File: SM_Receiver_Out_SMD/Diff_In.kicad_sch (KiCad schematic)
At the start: 9 parts, among them J7 RJ45, J8 RJ45, SW2 Terminators, U3 AM26C32IN

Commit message: working on BOM
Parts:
- added R2: 100K, Resistor_SMD:R_0603_1608Metric_Pad0.98x0.95mm_HandSolder, symbol Device:R
- J7, J8: LCSC_PN (none) -> C305972
- SW2: Digi-Key_PN (none) -> 2223-DS04-254-1L-04BK-ND; LCSC_PN (none) -> C509571; MPN (none) -> DS04-254-1L-04BK
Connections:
- net GND: now also R2.2; no longer U3.12 (EN_2)
- new net DIFF_EN: R2.1, U3.12 (EN_2)
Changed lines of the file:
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@@
     (stroke (width 0) (type default) (color 0 0 0 0))
   )
-  (wire (pts (xy 109.855 116.84) (xy 109.855 128.905))
+  (wire (pts (xy 108.204 116.84) (xy 121.92 116.84))
     (stroke (width 0) (type default) (color 0 0 0 0))
   )
-  (wire (pts (xy 121.92 116.84) (xy 109.855 116.84))
-    (stroke (width 0) (type default) (color 0 0 0 0))
-  )
   (global_label "Serial1_P" (shape input) (at 121.92 121.92 180) (fields_autoplaced)
     (effects (font (size 1.27 1.27)) (justify right))
@@
     (property "Intersheet References" "${INTERSHEET_REFS}" (id 0) (at 229.7147 62.3094 0)
       (effects (font (size 1.27 1.27)) (justify left) hide)
+    )
+  )
+  (global_label "DIFF_EN" (shape input) (at 108.204 116.84 180) (fields_autoplaced)
+    (effects (font (size 1.27 1.27)) (justify right))
+    (property "Intersheet References" "${INTERSHEET_REFS}" (id 0) (at 98.3808 116.7606 0)
+      (effects (font (size 1.27 1.27)) (justify right) hide)
     )
   )
@@
       (effects (font (size 1.27 1.27)) hide)
     )
+    (property "LCSC_PN" "C305972" (id 6) (at 147.32 53.34 0)
+      (effects (font (size 1.27 1.27)) hide)
+    )
     (pin "1")
     (pin "2")
@@
     (pin "8")
   )
-  (symbol (lib_id "power:GND") (at 109.855 128.905 0) (mirror y) (unit 1)
-    (in_bom yes) (on_board yes) (fields_autoplaced)
-    (property "Reference" "#PWR018" (id 0) (at 109.855 135.255 0)
-      (effects (font (size 1.27 1.27)) hide)
-    )
-    (property "Value" "GND" (id 1) (at 109.855 134.493 0))
-    (property "Footprint" "" (id 2) (at 109.855 128.905 0)
-      (effects (font (size 1.27 1.27)) hide)
-    )
-    (property "Datasheet" "" (id 3) (at 109.855 128.905 0)
+  (symbol (lib_id "power:GND") (at 108.204 124.46 0) (mirror y) (unit 1)
+    (in_bom yes) (on_board yes)
+    (property "Reference" "#PWR018" (id 0) (at 108.204 130.81 0)
+      (effects (font (size 1.27 1.27)) hide)
+    )
+    (property "Value" "GND" (id 1) (at 108.204 128.27 0))
+    (property "Footprint" "" (id 2) (at 108.204 124.46 0)
+      (effects (font (size 1.27 1.27)) hide)
+    )
+    (property "Datasheet" "" (id 3) (at 108.204 124.46 0)
       (effects (font (size 1.27 1.27)) hide)
     )
@@
     (pin "2")
   )
+  (symbol (lib_id "Device:R") (at 108.204 120.65 0) (unit 1)
+    (in_bom yes) (on_board yes)
+    (property "Reference" "R2" (id 0) (at 102.108 120.142 0)
+      (effects (font (size 1.27 1.27)) (justify left))
+    )
+    (property "Value" "100K" (id 1) (at 101.346 122.174 0)
+      (effects (font (size 1.27 1.27)) (justify left))
+    )
+    (property "Footprint" "Resistor_SMD:R_0603_1608Metric_Pad0.98x0.95mm_HandSolder" (id 2) (at 106.426 120.65 90)
+      (effects (font (size 1.27 1.27)) hide)
+    )
+    (property "Datasheet" "~" (id 3) (at 108.204 120.65 0)
+      (effects (font (size 1.27 1.27)) hide)
+    )
+    (property "Digi-Key_PN" "YAG1235CT-ND" (id 4) (at 108.204 120.65 0)
+      (effects (font (size 1.27 1.27)) hide)
+    )
+    (property "LCSC_PN" "C25803" (id 5) (at 108.204 120.65 0)
+      (effects (font (size 1.27 1.27)) hide)
+    )
+    (property "MPN" "RT0603BRD07100KL" (id 6) (at 108.204 120.65 0)
+      (effects (font (size 1.27 1.27)) hide)
+    )
+    (pin "1")
+    (pin "2")
+  )
   (symbol (lib_id "power:+3.3V") (at 186.055 104.775 0) (mirror y) (unit 1)
     (in_bom yes) (on_board yes) (fields_autoplaced)
@@
     )
     (property "Datasheet" "~" (id 3) (at 203.2 67.31 0)
+      (effects (font (size 1.27 1.27)) hide)
+    )
+    (property "Digi-Key_PN" "2223-DS04-254-1L-04BK-ND" (id 4) (at 203.2 67.31 0)
+      (effects (font (size 1.27 1.27)) hide)
+    )
+    (property "LCSC_PN" "C509571" (id 5) (at 203.2 67.31 0)
+      (effects (font (size 1.27 1.27)) hide)
+    )
+    (property "MPN" "DS04-254-1L-04BK" (id 6) (at 203.2 67.31 0)
       (effects (font (size 1.27 1.27)) hide)
     )
@@
       (effects (font (size 1.27 1.27)) hide)
     )
+    (property "LCSC_PN" "C305972" (id 6) (at 111.76 53.34 0)
+      (effects (font (size 1.27 1.27)) hide)
+    )

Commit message: fixing I2C lines were backwards
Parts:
- C4: Digi-Key_PN 1292-1630-1-ND -> 1276-1935-2-ND; LCSC_PN C1525 -> C14663; MPN 0402B104K160CT -> CL10B104KB8NNWC
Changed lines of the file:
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@@
       (effects (font (size 1.27 1.27)) hide)
     )
-    (property "Digi-Key_PN" "1292-1630-1-ND" (id 4) (at 186.055 108.585 0)
+    (property "Digi-Key_PN" "1276-1935-2-ND" (id 4) (at 186.055 108.585 0)
       (effects (font (size 1.27 1.27)) hide)
     )
-    (property "MPN" "0402B104K160CT" (id 5) (at 186.055 108.585 0)
+    (property "MPN" "CL10B104KB8NNWC" (id 5) (at 186.055 108.585 0)
       (effects (font (size 1.27 1.27)) hide)
     )
-    (property "LCSC_PN" "C1525" (id 6) (at 186.055 108.585 0)
+    (property "LCSC_PN" "C14663" (id 6) (at 186.055 108.585 0)
       (effects (font (size 1.27 1.27)) hide)
     )

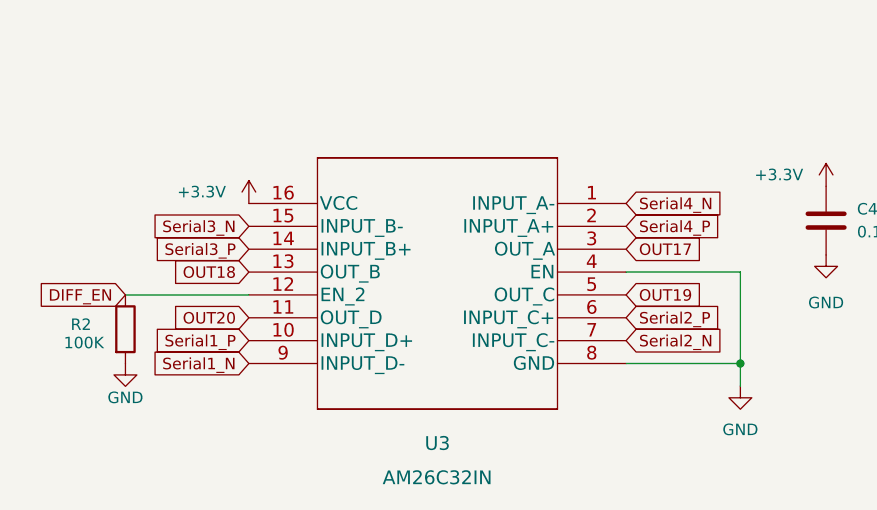
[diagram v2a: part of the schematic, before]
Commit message: fix miswired serial receiver
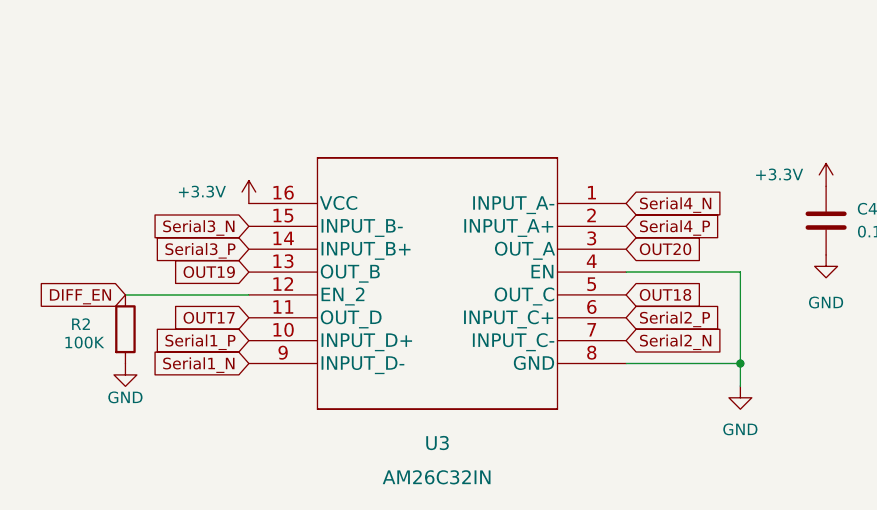
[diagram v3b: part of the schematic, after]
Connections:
- net OUT17: now also U3.11 (OUT_D); no longer U3.3 (OUT_A)
- net OUT18: now also U3.5 (OUT_C); no longer U3.13 (OUT_B)
- net OUT19: now also U3.13 (OUT_B); no longer U3.5 (OUT_C)
- net OUT20: now also U3.3 (OUT_A); no longer U3.11 (OUT_D)
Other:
- title: Receiver Out SMD -> SM Receiver Out SMD
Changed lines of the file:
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@@
   (paper "A4")
   (title_block
-    (title "Receiver Out SMD")
-    (date "2021-08-29")
-    (rev "v1")
+    (title "SM Receiver Out SMD")
+    (date "2022-03-25")
+    (rev "v2")
   )
   (junction (at 176.53 124.46) (diameter 0) (color 0 0 0 0)
@@
     )
   )
-  (global_label "OUT18" (shape input) (at 121.92 114.3 180) (fields_autoplaced)
-    (effects (font (size 1.27 1.27)) (justify right))
-    (property "Intersheet References" "${INTERSHEET_REFS}" (id 0) (at 113.5482 114.2206 0)
-      (effects (font (size 1.27 1.27)) (justify right) hide)
-    )
-  )
-  (global_label "OUT20" (shape input) (at 121.92 119.38 180) (fields_autoplaced)
-    (effects (font (size 1.27 1.27)) (justify right))
-    (property "Intersheet References" "${INTERSHEET_REFS}" (id 0) (at 113.5482 119.3006 0)
-      (effects (font (size 1.27 1.27)) (justify right) hide)
+  (global_label "OUT18" (shape input) (at 163.83 116.84 0) (fields_autoplaced)
+    (effects (font (size 1.27 1.27)) (justify left))
+    (property "Intersheet References" "${INTERSHEET_REFS}" (id 0) (at 172.2018 116.9194 0)
+      (effects (font (size 1.27 1.27)) (justify left) hide)
+    )
+  )
+  (global_label "OUT20" (shape input) (at 163.83 111.76 0) (fields_autoplaced)
+    (effects (font (size 1.27 1.27)) (justify left))
+    (property "Intersheet References" "${INTERSHEET_REFS}" (id 0) (at 172.2018 111.8394 0)
+      (effects (font (size 1.27 1.27)) (justify left) hide)
     )
   )
@@
     )
   )
-  (global_label "OUT19" (shape input) (at 163.83 116.84 0) (fields_autoplaced)
-    (effects (font (size 1.27 1.27)) (justify left))
-    (property "Intersheet References" "${INTERSHEET_REFS}" (id 0) (at 172.2018 116.7606 0)
-      (effects (font (size 1.27 1.27)) (justify left) hide)
+  (global_label "OUT19" (shape input) (at 121.92 114.3 180) (fields_autoplaced)
+    (effects (font (size 1.27 1.27)) (justify right))
+    (property "Intersheet References" "${INTERSHEET_REFS}" (id 0) (at 113.5482 114.3794 0)
+      (effects (font (size 1.27 1.27)) (justify right) hide)
     )
   )
@@
     )
   )
-  (global_label "OUT17" (shape input) (at 163.83 111.76 0) (fields_autoplaced)
-    (effects (font (size 1.27 1.27)) (justify left))
-    (property "Intersheet References" "${INTERSHEET_REFS}" (id 0) (at 172.2018 111.6806 0)
-      (effects (font (size 1.27 1.27)) (justify left) hide)
-    )
-  )
+  (global_label "OUT17" (shape input) (at 121.92 119.38 180) (fields_autoplaced)
+    (effects (font (size 1.27 1.27)) (justify right))
+    (property "Intersheet References" "${INTERSHEET_REFS}" (id 0) (at 113.5482 119.4594 0)
+      (effects (font (size 1.27 1.27)) (justify right) hide)
+    )
+  )

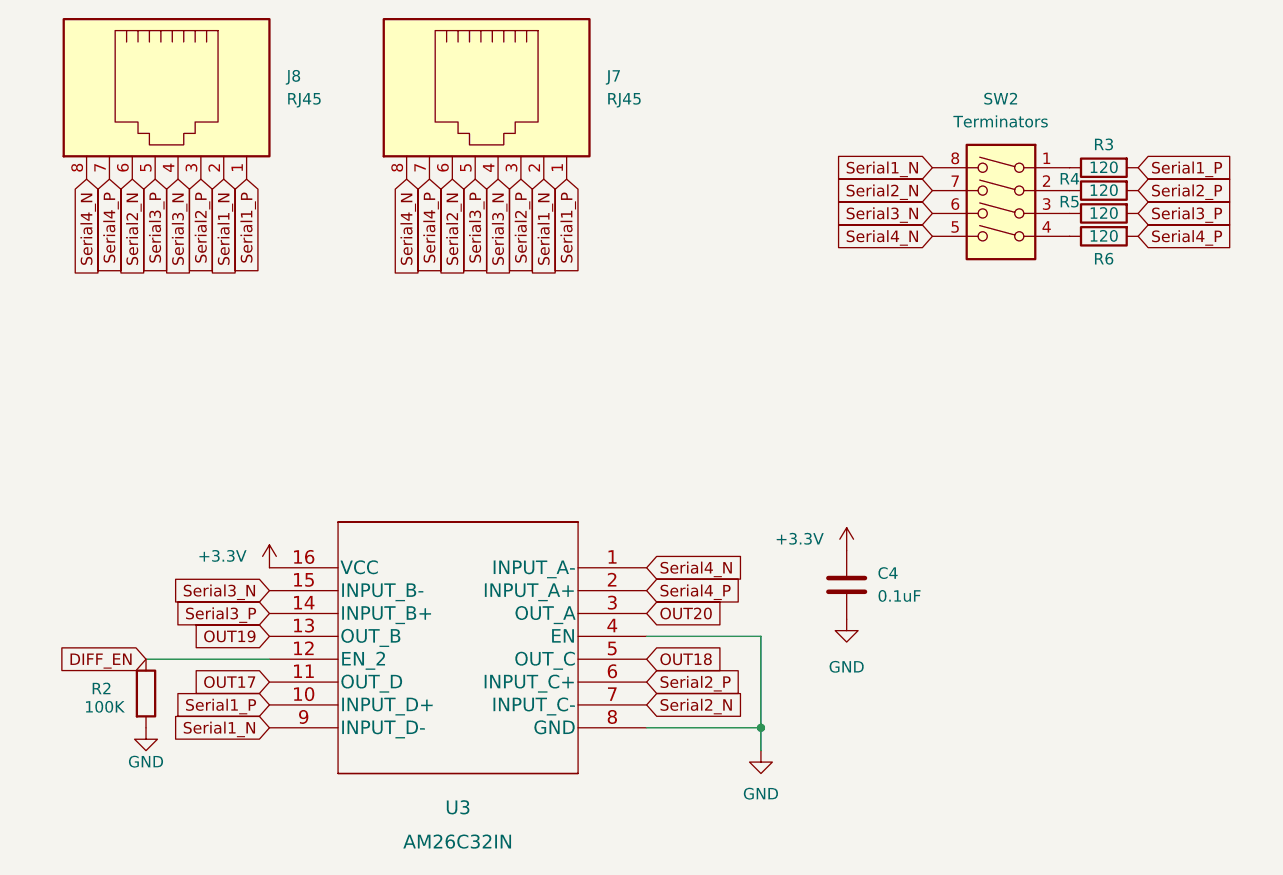
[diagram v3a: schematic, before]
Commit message: added 100 ohms to lines
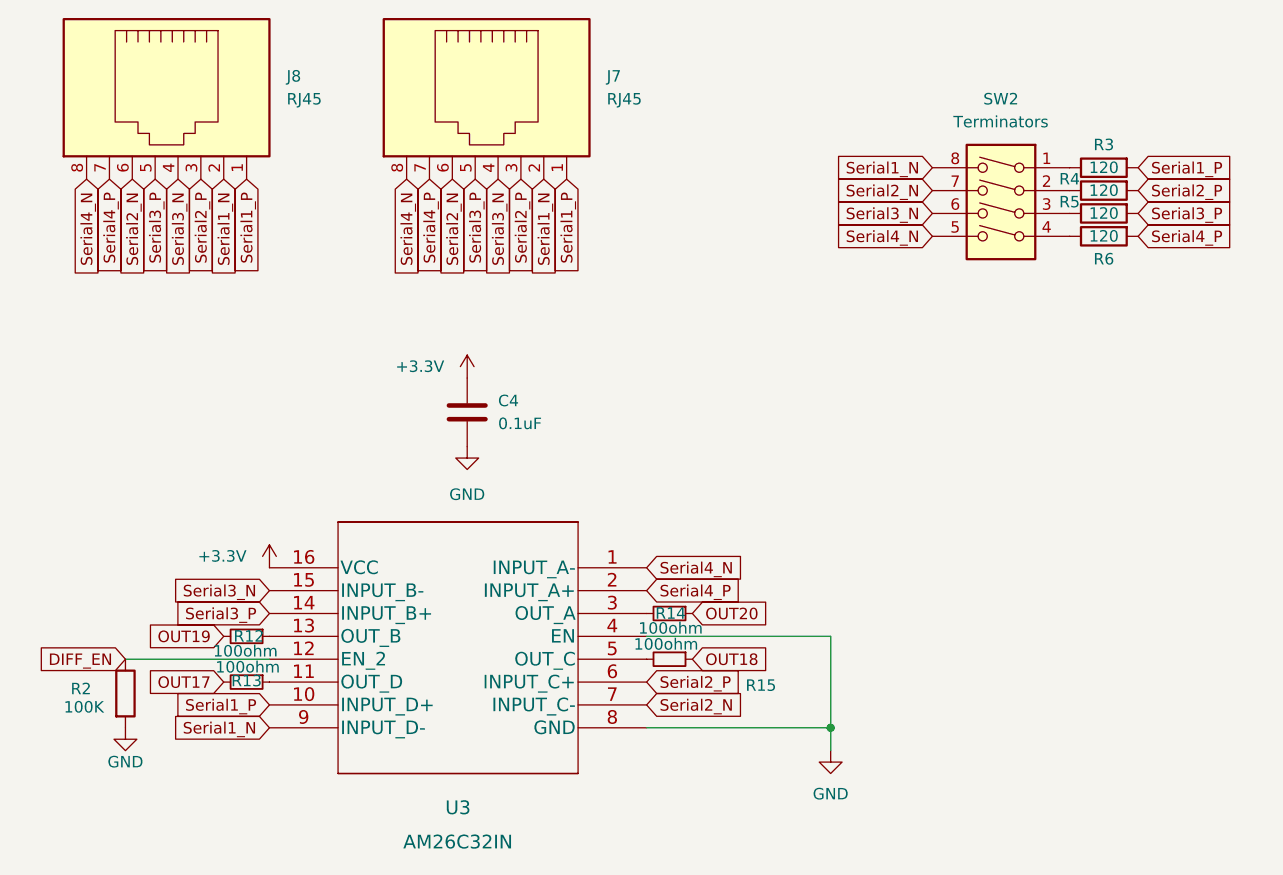
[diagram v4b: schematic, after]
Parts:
- added R12, R13, R14, R15: 100ohm, Resistor_SMD:R_0603_1608Metric_Pad0.98x0.95mm_HandSolder, symbol Device:R_Small
- U3: footprint Package_SO:SOIC-16_3.9x9.9mm_P1.27mm -> (none)
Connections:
- net OUT17: now also R13.2; no longer U3.11 (OUT_D)
- net OUT18: now also R15.1; no longer U3.5 (OUT_C)
- net OUT19: now also R12.2; no longer U3.13 (OUT_B)
- net OUT20: now also R14.1; no longer U3.3 (OUT_A)
- new net: R13.1, U3.11 (OUT_D)
- new net: R12.1, U3.13 (OUT_B)
- new net: R14.2, U3.3 (OUT_A)
- new net: R15.2, U3.5 (OUT_C)
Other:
- moved on the sheet: C4, R2

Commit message: i think Kicad has a bug
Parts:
- R14, R15: Digi-Key_PN (none) -> 311-100HRCT-ND; MPN (none) -> RC0603FR-07100RL
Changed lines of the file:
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@@
       (effects (font (size 1.27 1.27)) hide)
     )
-    (property "Digi-Key_PN" "" (id 5) (at 166.37 116.84 0)
+    (property "Digi-Key_PN" "311-100HRCT-ND" (id 5) (at 166.37 116.84 0)
       (effects (font (size 1.27 1.27)) hide)
     )
-    (property "MPN" "" (id 6) (at 166.37 116.84 0)
+    (property "MPN" "RC0603FR-07100RL" (id 6) (at 166.37 116.84 0)
       (effects (font (size 1.27 1.27)) hide)
     )
@@
       (effects (font (size 1.27 1.27)) hide)
     )
-    (property "Digi-Key_PN" "" (id 5) (at 166.37 111.76 0)
+    (property "Digi-Key_PN" "311-100HRCT-ND" (id 5) (at 166.37 111.76 0)
       (effects (font (size 1.27 1.27)) hide)
     )
-    (property "MPN" "" (id 6) (at 166.37 111.76 0)
+    (property "MPN" "RC0603FR-07100RL" (id 6) (at 166.37 111.76 0)
       (effects (font (size 1.27 1.27)) hide)
     )
